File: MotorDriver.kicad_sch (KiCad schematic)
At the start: 14 parts, among them U4 DRV8323HRTAR

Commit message: Add proper footprints
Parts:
- C18, C19, C20, C21, C23: footprint (none) -> Capacitor_SMD:C_0603_1608Metric
- C22: footprint (none) -> Capacitor_THT:CP_Radial_D4.0mm_P1.50mm
- R8, R9: footprint (none) -> Resistor_SMD:R_0603_1608Metric
- U4: footprint QFN50P600X600X80-41N-D -> ext_footprint:QFN50P600X600X80-41N-D
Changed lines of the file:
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@@
       (effects (font (size 1.27 1.27)) (justify right))
     )
-    (property "Footprint" "" (at 129.8448 52.07 0)
+    (property "Footprint" "Capacitor_SMD:C_0603_1608Metric" (at 129.8448 52.07 0)
       (effects (font (size 1.27 1.27)) hide)
     )
@@
       (effects (font (size 1.27 1.27)) (justify left))
     )
-    (property "Footprint" "" (at 67.0052 113.03 0)
+    (property "Footprint" "Capacitor_THT:CP_Radial_D4.0mm_P1.50mm" (at 67.0052 113.03 0)
       (effects (font (size 1.27 1.27)) hide)
     )
@@
       (effects (font (size 1.27 1.27)) (justify left))
     )
-    (property "Footprint" "" (at 155.702 101.6 90)
+    (property "Footprint" "Resistor_SMD:R_0603_1608Metric" (at 155.702 101.6 90)
       (effects (font (size 1.27 1.27)) hide)
     )
@@
       (effects (font (size 1.27 1.27)))
     )
-    (property "Footprint" "" (at 146.05 74.168 90)
+    (property "Footprint" "Resistor_SMD:R_0603_1608Metric" (at 146.05 74.168 90)
       (effects (font (size 1.27 1.27)) hide)
     )
@@
       (effects (font (size 1.27 1.27)) (justify left))
     )
-    (property "Footprint" "" (at 55.5752 113.03 0)
+    (property "Footprint" "Capacitor_SMD:C_0603_1608Metric" (at 55.5752 113.03 0)
       (effects (font (size 1.27 1.27)) hide)
     )
@@
       (effects (font (size 1.27 1.27)))
     )
-    (property "Footprint" "QFN50P600X600X80-41N-D" (at 139.7 77.47 0)
+    (property "Footprint" "ext_footprint:QFN50P600X600X80-41N-D" (at 139.7 77.47 0)
       (effects (font (size 1.27 1.27)) (justify left) hide)
     )
@@
       (effects (font (size 1.27 1.27)) (justify left))
     )
-    (property "Footprint" "" (at 158.4452 116.84 0)
+    (property "Footprint" "Capacitor_SMD:C_0603_1608Metric" (at 158.4452 116.84 0)
       (effects (font (size 1.27 1.27)) hide)
     )
@@
       (effects (font (size 1.27 1.27)) (justify left))
     )
-    (property "Footprint" "" (at 93.6752 95.25 0)
+    (property "Footprint" "Capacitor_SMD:C_0603_1608Metric" (at 93.6752 95.25 0)
       (effects (font (size 1.27 1.27)) hide)
     )
@@
       (effects (font (size 1.27 1.27)) (justify left))
     )
-    (property "Footprint" "" (at 77.1652 105.41 0)
-      (effects (font (size 1.27 1.27)) hide)
-    )
+    (property "Footprint" "Capacitor_SMD:C_0603_1608Metric" (at 77.1652 105.41 0)
+      (effects (font (size 1.27 1.27)) hide)
+    )

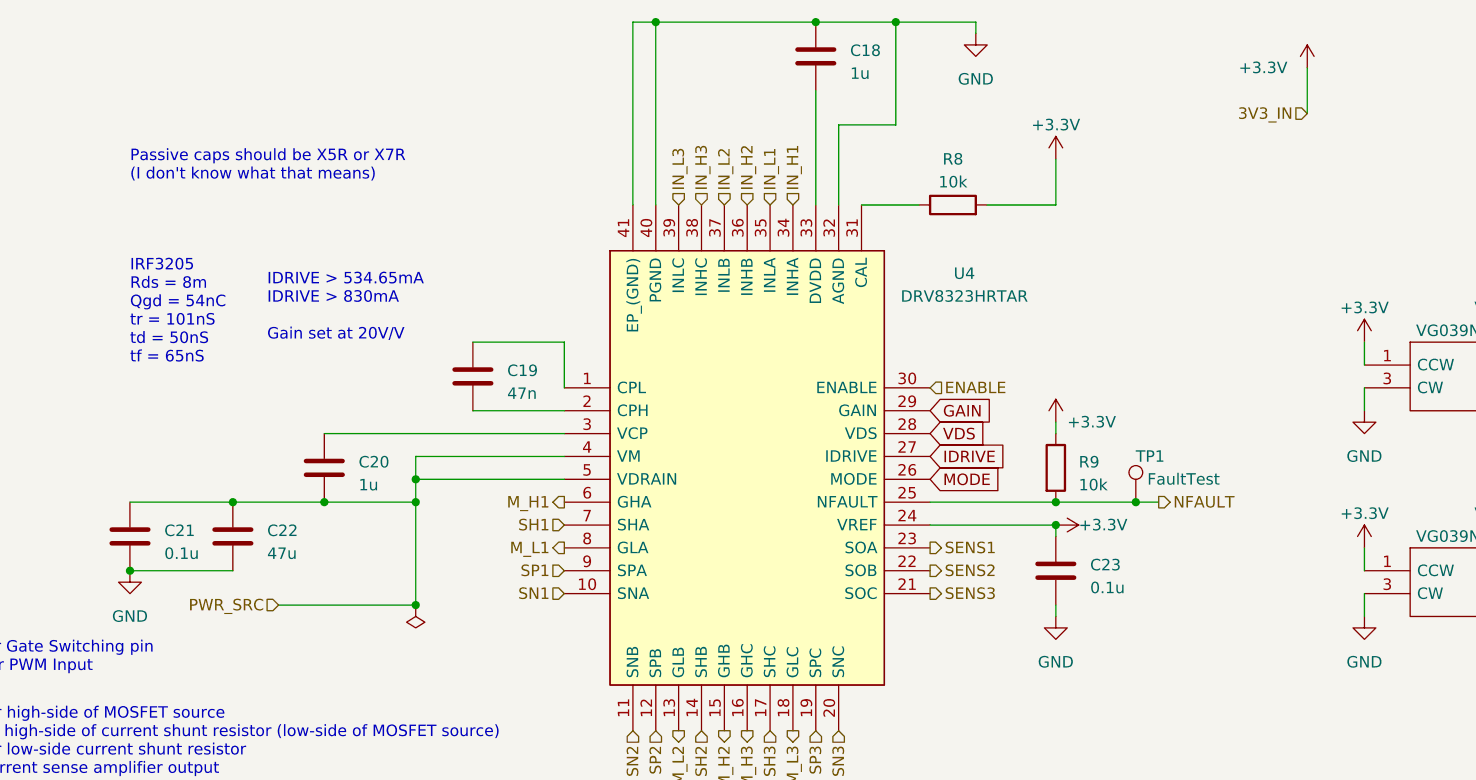
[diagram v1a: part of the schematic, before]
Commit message: Add proper JST Connector
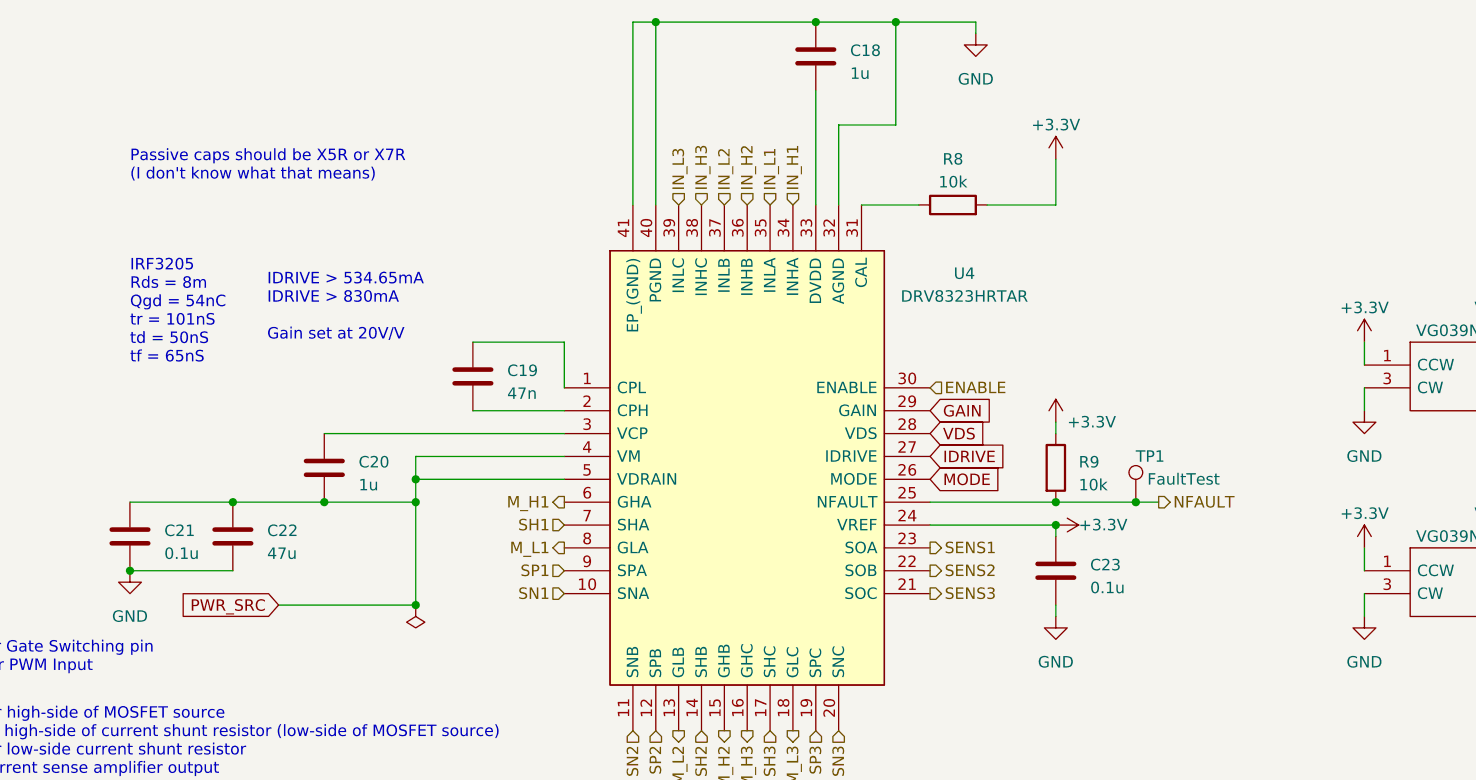
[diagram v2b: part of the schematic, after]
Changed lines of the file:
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@@
-    (stroke (width 0) (type default))
-  )
-  (wire (pts (xy 185.42 62.23) (xy 185.42 57.15))
     (stroke (width 0) (type default))
   )
@@
     )
   )
+  (global_label "PWR_SRC" (shape input) (at 71.12 116.84 180) (fields_autoplaced)
+    (effects (font (size 1.27 1.27)) (justify right))
+    (property "Intersheetrefs" "${INTERSHEET_REFS}" (at 59.5057 116.84 0)
+      (effects (font (size 1.27 1.27)) (justify right) hide)
+    )
+  )
   (global_label "GAIN" (shape input) (at 219.71 90.17 0) (fields_autoplaced)
     (effects (font (size 1.27 1.27)) (justify left))
@@
     (effects (font (size 1.27 1.27)) (justify right))
   )
-  (hierarchical_label "PWR_SRC" (shape input) (at 71.12 116.84 180) (fields_autoplaced)
-    (effects (font (size 1.27 1.27)) (justify right))
-  )
   (hierarchical_label "M_H2" (shape output) (at 120.65 130.81 270) (fields_autoplaced)
     (effects (font (size 1.27 1.27)) (justify right))
@@
   (hierarchical_label "IN_H1" (shape input) (at 128.27 72.39 90) (fields_autoplaced)
     (effects (font (size 1.27 1.27)) (justify left))
-  )
-  (hierarchical_label "3V3_IN" (shape input) (at 185.42 62.23 180) (fields_autoplaced)
-    (effects (font (size 1.27 1.27)) (justify right))
   )
   (hierarchical_label "SN3" (shape input) (at 133.35 130.81 270) (fields_autoplaced)
@@
         )
       )
-    )
-  )
-  (symbol (lib_id "power:+3.3V") (at 185.42 57.15 0) (unit 1)
-    (in_bom yes) (on_board yes) (dnp no)
-    (property "Reference" "#PWR048" (at 185.42 60.96 0)
-      (effects (font (size 1.27 1.27)) hide)
-    )
-    (property "Value" "+3.3V" (at 177.8 57.15 0)
-      (effects (font (size 1.27 1.27)) (justify left))
-    )
-    (property "Footprint" "" (at 185.42 57.15 0)
-      (effects (font (size 1.27 1.27)) hide)
-    )
-    (property "Datasheet" "" (at 185.42 57.15 0)
-      (effects (font (size 1.27 1.27)) hide)
-    )
-    (pin "1")
-    (instances
-      (project "electrium-esc-v2"
-        (path "/be00c12c-11fa-42cb-8a0b-46fcd24b2ced/7b8d4e0f-f5b3-4d23-9d20-d147bb4bf07d"
-          (reference "#PWR048") (unit 1)
-        )
-      )

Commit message: fixed ERC violations
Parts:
- VR1, VR2, VR3, VR4: footprint VG039NCHXTB204 -> VG039NCHXTB204:VG039NCHXTB204
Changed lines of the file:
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@@
       (effects (font (size 1.27 1.27)))
     )
-    (property "Footprint" "VG039NCHXTB204" (at 254 110.49 0)
+    (property "Footprint" "VG039NCHXTB204:VG039NCHXTB204" (at 254 110.49 0)
       (effects (font (size 1.27 1.27)) (justify left) hide)
     )
@@
       (effects (font (size 1.27 1.27)))
     )
-    (property "Footprint" "VG039NCHXTB204" (at 215.9 87.63 0)
+    (property "Footprint" "VG039NCHXTB204:VG039NCHXTB204" (at 215.9 87.63 0)
       (effects (font (size 1.27 1.27)) (justify left) hide)
     )
@@
       (effects (font (size 1.27 1.27)))
     )
-    (property "Footprint" "VG039NCHXTB204" (at 254 87.63 0)
+    (property "Footprint" "VG039NCHXTB204:VG039NCHXTB204" (at 254 87.63 0)
       (effects (font (size 1.27 1.27)) (justify left) hide)
     )
@@
       (effects (font (size 1.27 1.27)))
     )
-    (property "Footprint" "VG039NCHXTB204" (at 215.9 110.49 0)
-      (effects (font (size 1.27 1.27)) (justify left) hide)
-    )
+    (property "Footprint" "VG039NCHXTB204:VG039NCHXTB204" (at 215.9 110.49 0)
+      (effects (font (size 1.27 1.27)) (justify left) hide)
+    )
